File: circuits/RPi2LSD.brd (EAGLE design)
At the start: 65 x 56 mm, 36 parts, among them K1 PIN20X2

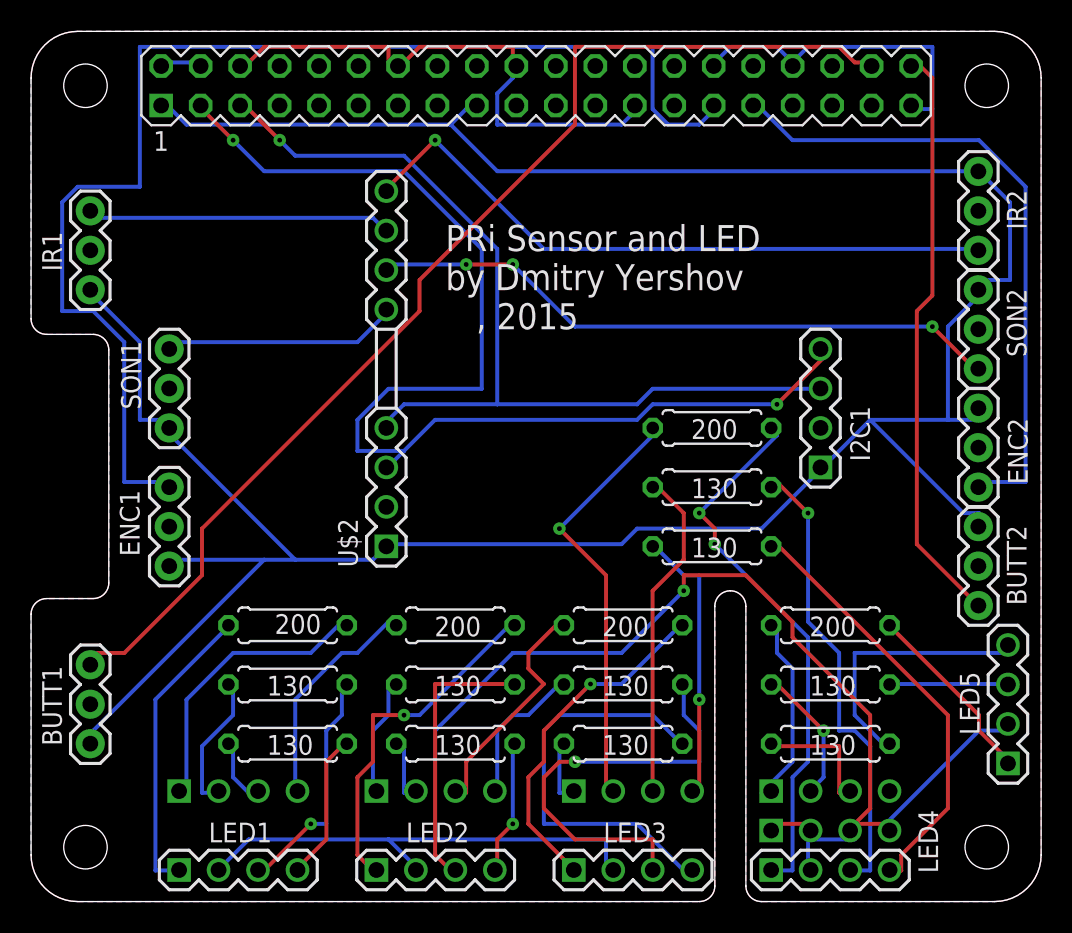
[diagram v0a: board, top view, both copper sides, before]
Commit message: Updated circuit boards. Use .brd file for OSH jobs.
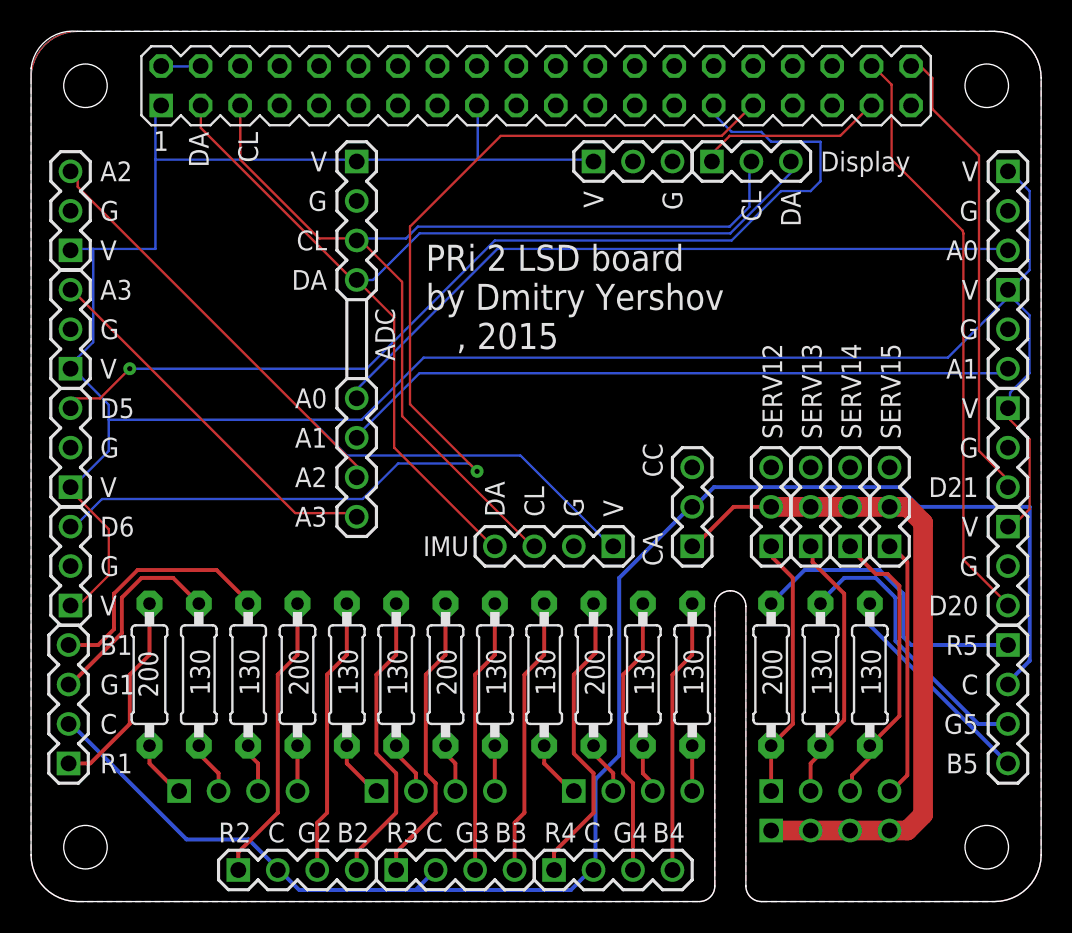
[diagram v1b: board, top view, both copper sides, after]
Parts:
- removed I2C1: (no value), cambridge_garage_electronics:1X04
- removed U$2: I2C_ADS115, cambridge_garage_electronics:I2C_AX4
- added ADC: I2C_ADS115, cambridge_garage_electronics:I2C_AX4
- added CA/CC, D_COMM, D_PWR, SERV12, SERV13, SERV14, SERV15: (no value), cambridge_garage_electronics:1X03
- added IMU: (no value), cambridge_garage_electronics:1X04
- BUTT1, BUTT2, ENC1, ENC2, IR1, IR2, SON1, SON2: device SparkFun-Connectors:1X03 -> cambridge_garage_electronics:1X03
- R1_BLUE, R1_GREEN, R1_RED, R2_BLUE, R2_GREEN, R2_RED, R3_BLUE, R3_GREEN, R3_RED, R4_BLUE, R4_GREEN, R4_RED, R5_BLUE, R5_GREEN, R5_RED: device adafruit:0207/7 -> adafruit:0207/9
- moved BUTT1 60.7 mm to (62.9, 24.1), turned to 270 degrees
- moved ENC2 59.8 mm to (2.54, 19.1), turned to 90 degrees
- moved IR2 59.8 mm to (2.54, 34.3), turned to 90 degrees
- moved SON1 56.4 mm to (62.9, 47.0), turned to 270 degrees
- moved R4_RED 17.6 mm to (36.2, 14.6), turned to 270 degrees
- moved LED4 14.0 mm to (33.7, 2.03)
- moved R4_GREEN 12.9 mm to (39.4, 14.6), turned to 270 degrees
- moved R3_RED 11.9 mm to (26.7, 14.6), turned to 270 degrees
- moved LED3 11.4 mm to (23.5, 2.03)
- moved R2_RED 10.6 mm to (17.1, 14.6), turned to 270 degrees
- moved LED1 9.88 mm to (2.41, 8.89), turned to 90 degrees
- moved R1_RED 9.44 mm to (7.62, 14.6), turned to 270 degrees
- moved LED2 8.89 mm to (13.3, 2.03)
- moved R4_BLUE 8.35 mm to (42.5, 14.6), turned to 270 degrees
- moved R3_GREEN 8.28 mm to (29.8, 14.6), turned to 270 degrees
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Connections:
- removed net LED_SUPP: LED1.2, LED2.2, LED3.2, LED4.2, LED5.2, LED_SUPP.1, LED_SUPP.2, LED_SUPP.3, LED_SUPP.4
- new net +5V_2: CA/CC.1, LED_SUPP.1, LED_SUPP.2, LED_SUPP.3, LED_SUPP.4, SERV12.2, SERV13.2, SERV14.2, SERV15.2
- new net GPIO24: K1.18
- new net LED_COMM: CA/CC.2, LED1.2, LED2.2, LED3.2, LED4.2, LED5.2
- new net SERVO_4: PWM4.4, SERV15.1
- net +3V3: now also ADC.1, D_PWR.1, IMU.1; no longer I2C1.1, U$2.1
- net AIN0: now also ADC.5; no longer U$2.5
- net AIN1: now also ADC.6; no longer U$2.6
- net AIN2: now also ADC.7; no longer U$2.7
- net AIN3: now also ADC.8; no longer U$2.8
- net GND: now also ADC.2, CA/CC.3, D_PWR.3, IMU.2, SERV12.3, SERV13.3, SERV14.3, SERV15.3; no longer I2C1.2, U$2.2
- net GPIO26: now also D_COMM.1
- net I2C_SCL: now also ADC.3, D_COMM.2, IMU.3; no longer I2C1.3, U$2.4
- net I2C_SDA: now also ADC.4, D_COMM.3, IMU.4; no longer I2C1.4, U$2.3
- net LED5_BLUE: now also SERV14.1
- net LED5_GREEN: now also SERV13.1
- net LED5_RED: now also SERV12.1
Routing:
- net LED_SUPP: track 106.8 -> 0.00 mm, vias 1 -> 0
- net LED_COMM: track 0.00 -> 101.5 mm
- net GND: track 56.4 -> 0.25 mm
- net +5V_2: track 0.00 -> 45.5 mm
- net GPIO20: track 73.5 -> 38.7 mm
- net AIN0: track 15.5 -> 46.5 mm
- net GPIO6: track 42.0 -> 70.9 mm, vias 0 -> 1
- net LED4_RED: track 27.7 -> 3.45 mm, vias 1 -> 0
- net LED4_GREEN: track 22.1 -> 3.18 mm
- net AIN3: track 42.6 -> 24.6 mm, vias 1 -> 0
- net SERVO_4: track 0.00 -> 16.8 mm
- net N$12: track 35.4 -> 19.4 mm, vias 2 -> 0
- net LED4_BLUE: track 18.4 -> 2.92 mm, vias 1 -> 0
- net LED1_RED: track 18.9 -> 3.78 mm
- net GPIO5: track 80.3 -> 65.4 mm, vias 0 -> 1
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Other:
- outline, holes or cut-outs redrawn
- board text added: "A0"
- board text added: "A1"
- board text added: "A2"
- board text added: "A3"
- board text added: "B1"
- board text added: "B2"
- board text added: "B3"
- board text added: "B4"
- board text added: "B5"
- board text added: "C"
- board text added: "CA"
- board text added: "CC"
- board text added: "CL"
- board text added: "D20"
- board text added: "D21"
- board text added: "D5"
- board text added: "D6"
- board text added: "DA"
- board text added: "Display"
- board text added: "G"
- board text added: "G1"
- board text added: "G2"
- board text added: "G3"
- board text added: "G4"
- board text added: "G5"
- board text added: "PRi 2 LSD board by Dmitry Yershov , 2015"
- board text added: "R1"
- board text added: "R2"
- board text added: "R3"
- board text added: "R4"
- board text added: "R5"
- board text added: "RPi 2 LED, sensor, and display board Legend: V, G - Power (+3V and Ground) Ax - Analog input (x = 0..3) Dx - Digital input (x is GPIO No) Rx, Bx, Gx - RGB LED output (x = 1..5) C - LED common line CA, CC - Common anode/cathode LED DA, CL - I2C data and clock lines"
- board text added: "V"
- board text removed: "+3V"
- board text removed: "GND"
- board text removed: "PRi Sensor and LED by Dmitry Yershov , 2015"
- board text removed: "SIG"
